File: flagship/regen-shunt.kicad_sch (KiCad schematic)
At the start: 17 parts, among them J3 EXT_SHUNT, Q501 100V, U3 TLV1805, U4 TLV431

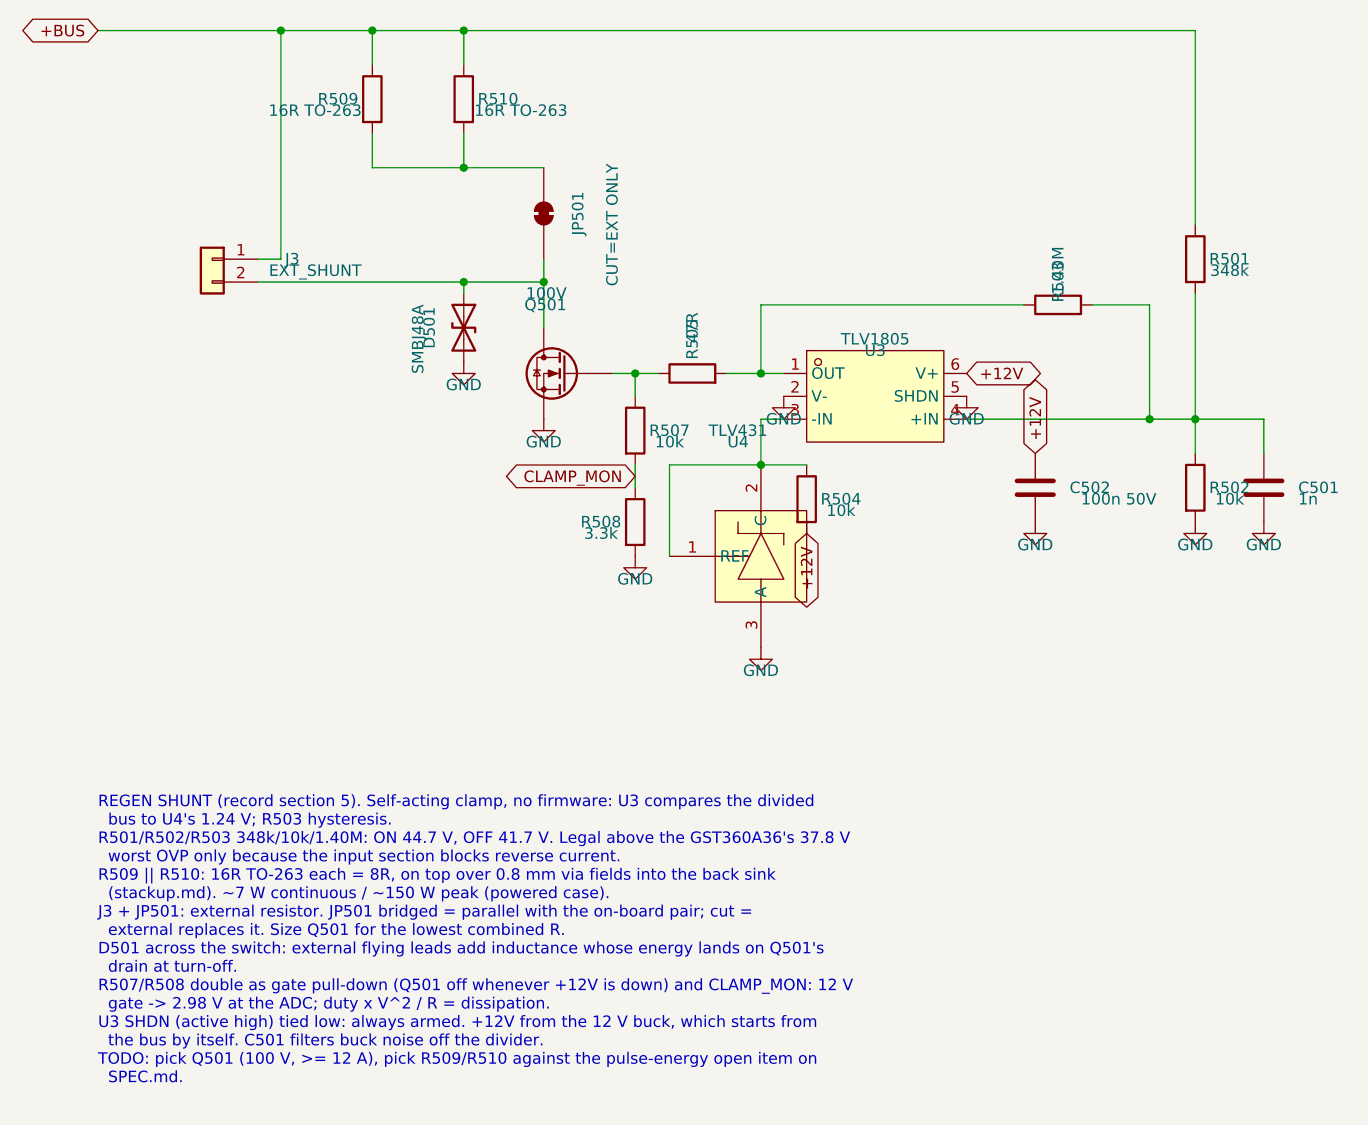
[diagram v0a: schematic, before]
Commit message: flagship: input protection detailed (LTC4364-1); real FETs and regen resistors picked
Input sheet drawn wired from the LTC4364 datasheet Figure 1 topology: 2.5 mOhm / 20 A
limit, 22 nF HGATE soft ramp, 100 nF timer, 51.5 V output clamp above the regen clamp,
UV 20 V / OV 50 V, 15 V gate zeners, SMBJ45CA bidirectional input TVS, 27k fault LED.
Verified: all input nets exact against the intended table; ERC 0 on the sheet.

Parts: PSMN3R7-100BSE (enhanced-SOA hot-swap D2PAK) in all five power FET positions,
DMN10H220L pre-charge FET, 3x Vishay D2TO35M 24 R regen resistors with isolated tabs to
GND. New project symbols with numbered pins matching the footprints: Q_NMOS_D2PAK
(1 G, 2 D tab, 3 S), Q_NMOS_SOT23 (1 G, 2 S, 3 D), R_D2PAK_TAB (resistor 1/3, tab 2).
Regen sheet regenerated for three resistors; nets exact. Motor CBST raised to 1 uF.
ERC: six of seven sheets at zero errors; Compute awaits GPIO assignment by layout.

Co-Authored-By: Claude Opus 5.5 (1M context) <noreply@anthropic.com>
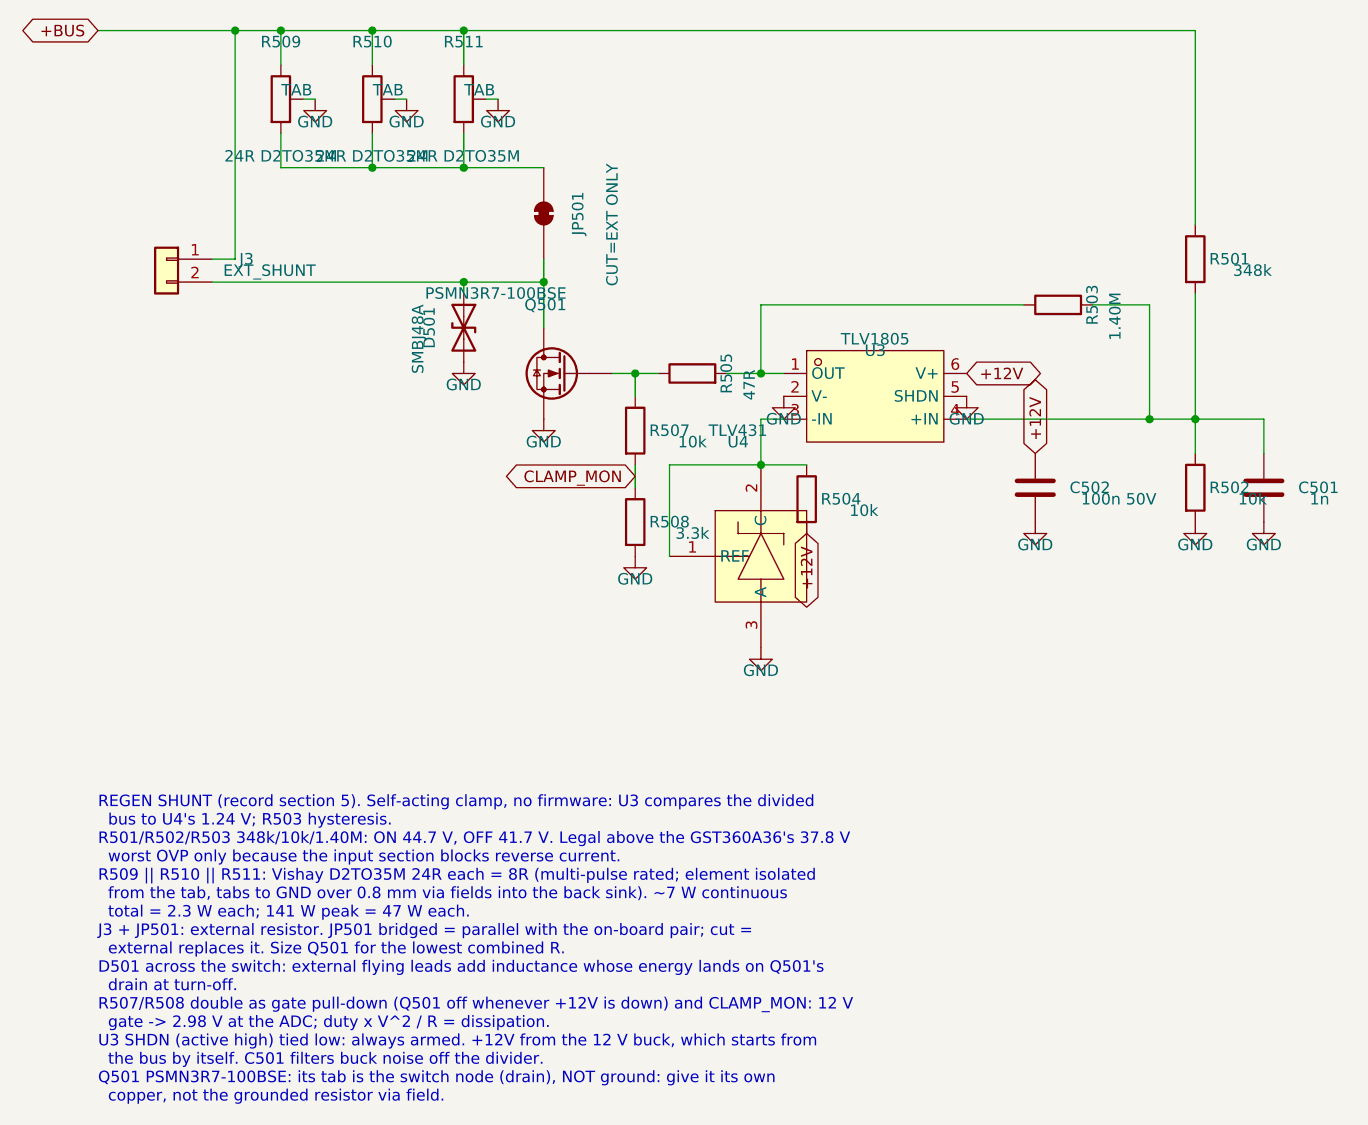
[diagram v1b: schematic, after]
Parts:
- removed Q501: 100V, symbol Device:Q_NMOS
- removed R509, R510: 16R TO-263, flagship:TO-263-2_L10.1-W8.8-P5.08-LS15.4-TL, symbol Device:R
- added Q501: PSMN3R7-100BSE, Package_TO_SOT_SMD:TO-263-2, symbol flagship:Q_NMOS_D2PAK
- added R509, R510, R511: 24R D2TO35M, Package_TO_SOT_SMD:TO-263-2, symbol flagship:R_D2PAK_TAB
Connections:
- net +BUS: now also R509.1, R510.1, R511.1
- net GND: now also Q501.3 (S), R509.2 (TAB), R510.2 (TAB), R511.2 (TAB)
- net at D501.1 (A1), J3.2 (Pin_2), JP501.1 (A): now also Q501.2 (D)
- net at R505.1, R507.1: now also Q501.1 (G)
- net at JP501.2 (B): now also R509.3, R510.3, R511.3
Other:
- note added: "REGEN SHUNT (record section 5). Self-acting clamp, no firmware: U3 compares the divided bus to U4's 1.24 V; R503 hysteresis. R501/R502/R503 348k/10k/1.40M: ON 44.7 V, OFF 41.7 V. Legal above the GST360A36's 37.8 V worst OVP only because the input section blocks reverse current. R509 || R510 || R511: Vishay D2TO35M 24R each = 8R (multi-pulse rated; element isolated from the tab, tabs to GND over 0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"
- note removed: "REGEN SHUNT (record section 5). Self-acting clamp, no firmware: U3 compares the divided bus to U4's 1.24 V; R503 hysteresis. R501/R502/R503 348k/10k/1.40M: ON 44.7 V, OFF 41.7 V. Legal above the GST360A36's 37.8 V worst OVP only because the input section blocks reverse current. R509 || R510: 16R TO-263 each = 8R, on top over 0.8 mm via fields into the back sink (stackup.md). ~7 W continuous / ~15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"

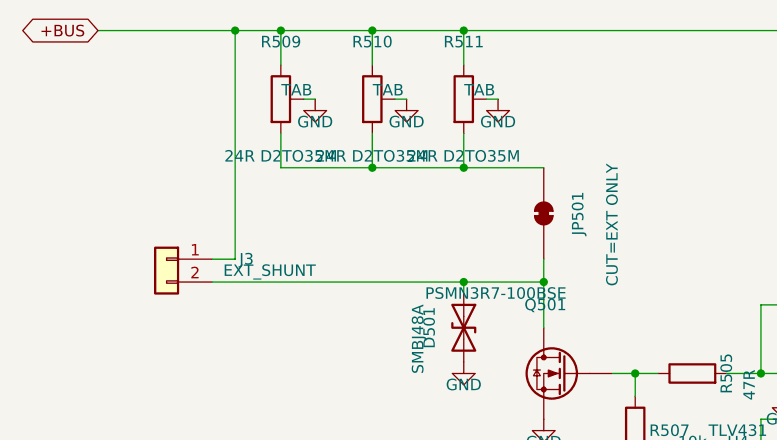
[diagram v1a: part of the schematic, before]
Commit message: flagship: Kelvin WSK2512 shunts everywhere (LTC4364 sense now 4-terminal), bulk and MLCC parts picked
R1 (LTC4364, 2.5 mOhm) becomes a 4-terminal shunt with SENSE and OUT on its Kelvin taps;
R1/R2/R401 all Vishay WSK2512 on the T2.21 mm footprint that value range needs. Bulk:
2x EEH-ZA1J101P 100 uF 63 V hybrid polymer + 2x GRM32ER72A225KA35L; buck input caps get
the same MLCC part number. Regen resistors labeled D2TO35M 24 R 2 %. Input nets verified
exact after regeneration; ERC 0 on every detailed sheet.

Co-Authored-By: Claude Opus 5.5 (1M context) <noreply@anthropic.com>
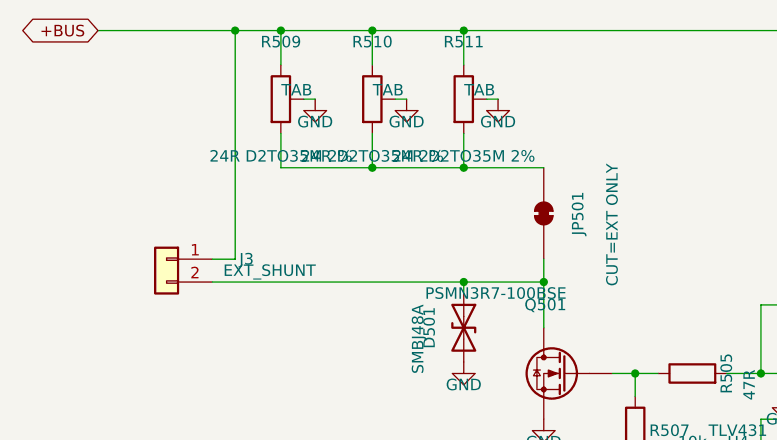
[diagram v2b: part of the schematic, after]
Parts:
- R509, R510, R511: value 24R D2TO35M -> 24R D2TO35M 2%
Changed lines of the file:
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@@
 			)
 		)
-		(property "Value" "24R D2TO35M"
+		(property "Value" "24R D2TO35M 2%"
 			(at 60.96 39.37 0)
 			(show_name no)
@@
 			)
 		)
-		(property "Value" "24R D2TO35M"
+		(property "Value" "24R D2TO35M 2%"
 			(at 40.64 39.37 0)
 			(show_name no)
@@
 			)
 		)
-		(property "Value" "24R D2TO35M"
+		(property "Value" "24R D2TO35M 2%"
 			(at 50.8 39.37 0)
 			(show_name no)
